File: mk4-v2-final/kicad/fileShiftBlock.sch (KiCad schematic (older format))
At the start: 2 parts, among them U4 74HC595, U5 74HC595

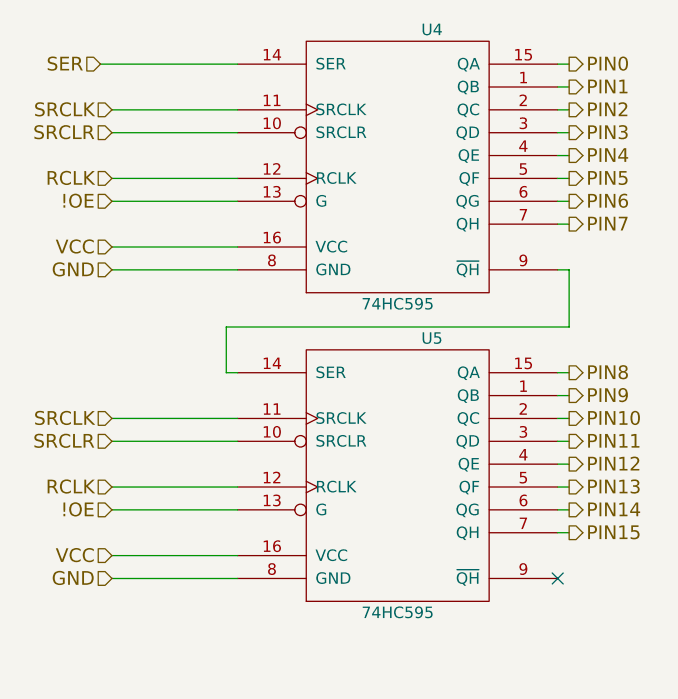
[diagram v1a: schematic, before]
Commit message: added headnight diodes, I don't think software control of them is going to be possible
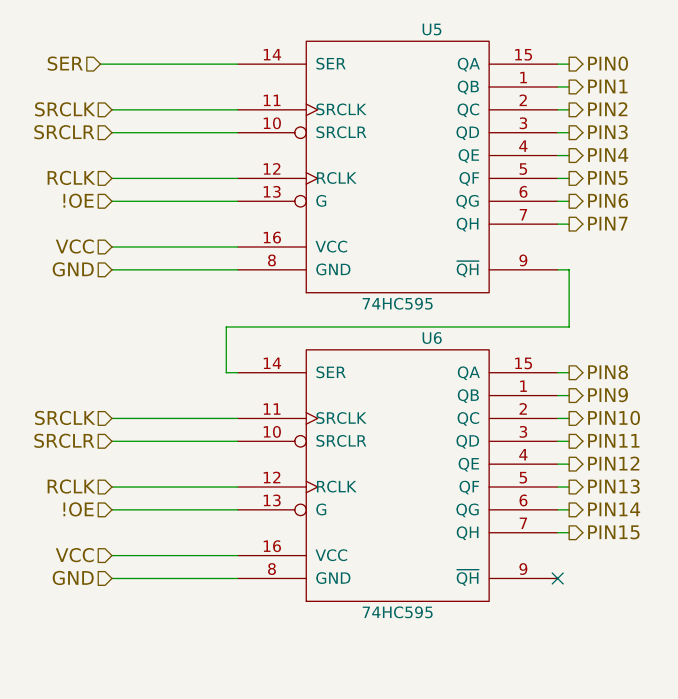
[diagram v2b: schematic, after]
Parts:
- renumbered U4 to U5, U5 to U6
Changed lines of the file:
@@
 $EndDescr
 $Comp
-L 74HC595-RESCUE-hitchco-mk4 U4
+L 74HC595-RESCUE-hitchco-mk4 U5
 U 1 1 5A664EEF
 P 5300 2950
-F 0 "U4" H 5450 3550 50  0000 C CNN
+F 0 "U5" H 5450 3550 50  0000 C CNN
 F 1 "74HC595" H 5300 2350 50  0000 C CNN
 F 2 "Housings_DIP:DIP-16_W7.62mm" H 5300 2950 50  0001 C CNN
@@
 	4600 3300 4050 3300
 $Comp
-L 74HC595-RESCUE-hitchco-mk4 U5
+L 74HC595-RESCUE-hitchco-mk4 U6
 U 1 1 5A26CD88
 P 5300 4300
-F 0 "U5" H 5450 4900 50  0000 C CNN
+F 0 "U6" H 5450 4900 50  0000 C CNN
 F 1 "74HC595" H 5300 3700 50  0000 C CNN
 F 2 "Housings_DIP:DIP-16_W7.62mm" H 5300 4300 50  0001 C CNN

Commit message: schematic is done, footprint association and netlist are also done
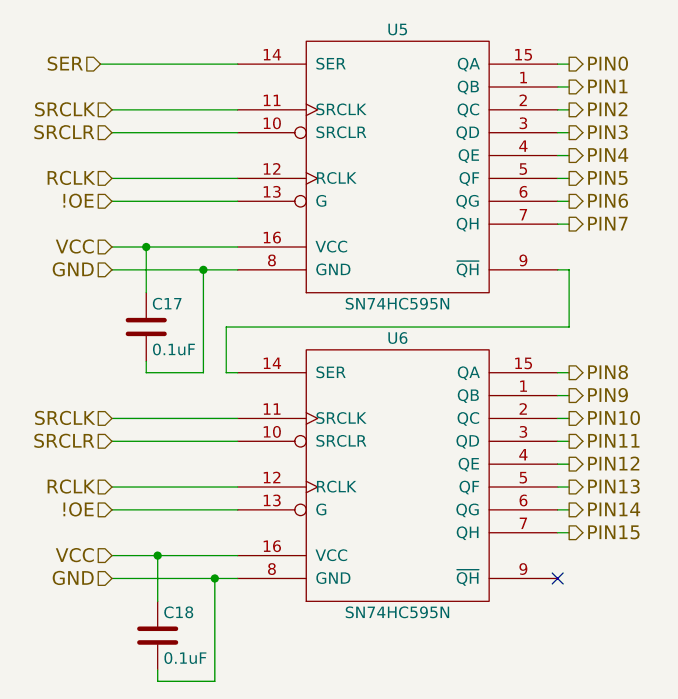
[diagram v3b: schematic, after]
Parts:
- removed U5, U6: 74HC595, Housings_DIP:DIP-16_W7.62mm, symbol 74HC595-RESCUE-hitchco-mk4
- added C17, C18: 0.1uF, C_Rect_L5.08mm_W3.175mm_P2.54mm:C_Rect_L5.08mm_W3.175mm_P2.54mm, symbol C
- added U5, U6: SN74HC595N, Housings_DIP:DIP-16_W7.62mm_Socket, symbol SN74HC595N
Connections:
- net !OE: now also U5.13 (G), U6.13 (G)
- net GND: now also C17.2, C18.2, U5.8 (GND), U6.8 (GND)
- net PIN0: now also U5.15 (QA)
- net PIN1: now also U5.1 (QB)
- net PIN10: now also U6.2 (QC)
- net PIN11: now also U6.3 (QD)
- net PIN12: now also U6.4 (QE)
- net PIN13: now also U6.5 (QF)
- net PIN14: now also U6.6 (QG)
- net PIN15: now also U6.7 (QH)
- net PIN2: now also U5.2 (QC)
- net PIN3: now also U5.3 (QD)
- net PIN4: now also U5.4 (QE)
- net PIN5: now also U5.5 (QF)
- net PIN6: now also U5.6 (QG)
- net PIN7: now also U5.7 (QH)
- net PIN8: now also U6.15 (QA)
- net PIN9: now also U6.1 (QB)
- net RCLK: now also U5.12 (RCLK), U6.12 (RCLK)
- net SER: now also U5.14 (SER)
- net SRCLK: now also U5.11 (SRCLK), U6.11 (SRCLK)
- net SRCLR: now also U5.10 (SRCLR), U6.10 (SRCLR)
- net VCC: now also C17.1, C18.1, U5.16 (VCC), U6.16 (VCC)
- new net: U5.9 (~QH), U6.14 (SER)
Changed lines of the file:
@@
 EESchema Schematic File Version 2
-LIBS:hitchco-mk4-rescue
 LIBS:power
 LIBS:device
@@
 LIBS:cd4013b
 LIBS:ncs3s1205sc
+LIBS:lca715
+LIBS:SN74HC595N
+LIBS:CD74HC4067
 LIBS:hitchco-mk4-cache
 EELAYER 25 0
@@
 $Descr A4 11693 8268
 encoding utf-8
-Sheet 45 54
+Sheet 38 54
 Title ""
 Date ""
@@
 $EndDescr
 $Comp
-L 74HC595-RESCUE-hitchco-mk4 U5
-U 1 1 5A664EEF
-P 5300 2950
-F 0 "U5" H 5450 3550 50  0000 C CNN
-F 1 "74HC595" H 5300 2350 50  0000 C CNN
-F 2 "Housings_DIP:DIP-16_W7.62mm" H 5300 2950 50  0001 C CNN
-F 3 "http://www.ti.com/lit/ds/symlink/sn74hc595.pdf" H 5300 2950 50  0001 C CNN
-	1    5300 2950
+L C C17
+U 1 1 5B1F2E84
+P 4200 3650
+F 0 "C17" H 4225 3750 50  0000 L CNN
+F 1 "0.1uF" H 4225 3550 50  0000 L CNN
+F 2 "C_Rect_L5.08mm_W3.175mm_P2.54mm:C_Rect_L5.08mm_W3.175mm_P2.54mm" H 4238 3500 50  0001 C CNN
+F 3 "http://datasheets.avx.com/AR-Series.pdf" H 4200 3650 50  0001 C CNN
+F 4 "478-5096-ND" H 4225 3850 50  0001 C CNN "digikey-pn"
+F 5 "AR205F104K4R" H 4225 3850 50  0001 C CNN "mfg-pn"
+	1    4200 3650
+	1    0    0    -1
+$EndComp
+$Comp
+L C C18
+U 1 1 5B1F2F7D
+P 4250 5000
+F 0 "C18" H 4275 5100 50  0000 L CNN
+F 1 "0.1uF" H 4275 4900 50  0000 L CNN
+F 2 "C_Rect_L5.08mm_W3.175mm_P2.54mm:C_Rect_L5.08mm_W3.175mm_P2.54mm" H 4288 4850 50  0001 C CNN
+F 3 "http://datasheets.avx.com/AR-Series.pdf" H 4250 5000 50  0001 C CNN
+F 4 "478-5096-ND" H 4275 5200 50  0001 C CNN "digikey-pn"
+F 5 "AR205F104K4R" H 4275 5200 50  0001 C CNN "mfg-pn"
+	1    4250 5000
 	1    0    0    -1
 $EndComp
@@
 Text HLabel 6050 3200 2    60   Output ~ 0
 PIN7
-Wire Wire Line
-	6000 3400 6050 3400
-Wire Wire Line
-	6050 3400 6050 3650
-Wire Wire Line
-	6050 3650 4550 3650
-Wire Wire Line
-	4550 3650 4550 3850
-Wire Wire Line
-	4550 3850 4600 3850
 Text HLabel 6050 3850 2    60   Output ~ 0
 PIN8
@@
 Text HLabel 6050 4550 2    60   Output ~ 0
 PIN15
-Wire Wire Line
-	6050 2500 6000 2500
-Wire Wire Line
-	6000 2600 6050 2600
-Wire Wire Line
-	6050 2700 6000 2700
-Wire Wire Line
-	6000 2800 6050 2800
-Wire Wire Line
-	6050 2900 6000 2900
-Wire Wire Line
-	6000 3000 6050 3000
-Wire Wire Line
-	6050 3100 6000 3100
-Wire Wire Line
-	6000 3200 6050 3200
-Wire Wire Line
-	6000 3950 6050 3950
-Wire Wire Line
-	6050 4050 6000 4050
-Wire Wire Line
-	6000 4150 6050 4150
-Wire Wire Line
-	6050 4250 6000 4250
-Wire Wire Line
-	6000 4350 6050 4350
-Wire Wire Line
-	6050 4450 6000 4450
-Wire Wire Line
-	6000 4550 6050 4550
 Text HLabel 4000 2500 0    60   Input ~ 0
 SER
-Wire Wire Line
-	4000 2500 4600 2500
 Text HLabel 4050 2700 0    60   Input ~ 0
 SRCLK
-Wire Wire Line
-	4050 2800 4600 2800
 Text HLabel 4050 3000 0    60   Input ~ 0
 RCLK
-Wire Wire Line
-	4050 3000 4600 3000
-Wire Wire Line
-	4050 2700 4600 2700
 Text HLabel 4050 2800 0    60   Input ~ 0
 SRCLR
 Text HLabel 4050 3100 0    60   Input ~ 0
 !OE
-Wire Wire Line
-	4050 3100 4600 3100
 Text HLabel 4050 3300 0    60   Input ~ 0
 VCC
 Text HLabel 4050 3400 0    60   Input ~ 0
 GND
-Wire Wire Line
-	4050 3400 4600 3400
-Wire Wire Line
-	4600 3300 4050 3300
-$Comp
-L 74HC595-RESCUE-hitchco-mk4 U6
-U 1 1 5A26CD88
-P 5300 4300
-F 0 "U6" H 5450 4900 50  0000 C CNN
-F 1 "74HC595" H 5300 3700 50  0000 C CNN
-F 2 "Housings_DIP:DIP-16_W7.62mm" H 5300 4300 50  0001 C CNN
-F 3 "http://www.ti.com/lit/ds/symlink/sn74hc595.pdf" H 5300 4300 50  0001 C CNN
-	1    5300 4300
-	1    0    0    -1
-$EndComp
 Text HLabel 4050 4050 0    60   Input ~ 0
 SRCLK
-Wire Wire Line
-	4050 4150 4600 4150
 Text HLabel 4050 4350 0    60   Input ~ 0
 RCLK
-Wire Wire Line
-	4050 4350 4600 4350
-Wire Wire Line
-	4050 4050 4600 4050
 Text HLabel 4050 4150 0    60   Input ~ 0
 SRCLR
 Text HLabel 4050 4450 0    60   Input ~ 0
 !OE
-Wire Wire Line
-	4050 4450 4600 4450
 Text HLabel 4050 4650 0    60   Input ~ 0
 VCC
@@
 GND
 Wire Wire Line
+	6000 3400 6050 3400
+Wire Wire Line
+	6050 3400 6050 3650
+Wire Wire Line
+	6050 3650 4550 3650
+Wire Wire Line
+	4550 3650 4550 3850
+Wire Wire Line
+	4550 3850 4600 3850
+Wire Wire Line
+	6050 2500 6000 2500
+Wire Wire Line
+	6000 2600 6050 2600
+Wire Wire Line
+	6050 2700 6000 2700
+Wire Wire Line
+	6000 2800 6050 2800
+Wire Wire Line
+	6050 2900 6000 2900
+Wire Wire Line
+	6000 3000 6050 3000
+Wire Wire Line
+	6050 3100 6000 3100
+Wire Wire Line
+	6000 3200 6050 3200
+Wire Wire Line
+	6000 3950 6050 3950
+Wire Wire Line
+	6050 4050 6000 4050
+Wire Wire Line
+	6000 4150 6050 4150
+Wire Wire Line
+	6050 4250 6000 4250
+Wire Wire Line
+	6000 4350 6050 4350
+Wire Wire Line
+	6050 4450 6000 4450
+Wire Wire Line
+	6000 4550 6050 4550
+Wire Wire Line
+	4000 2500 4600 2500
+Wire Wire Line
+	4050 2800 4600 2800
+Wire Wire Line
+	4050 3000 4600 3000
+Wire Wire Line
+	4050 2700 4600 2700
+Wire Wire Line
+	4050 3100 4600 3100
+Wire Wire Line
+	4050 3400 4600 3400
+Wire Wire Line
+	4600 3300 4050 3300
+Wire Wire Line
+	4050 4150 4600 4150
+Wire Wire Line
+	4050 4350 4600 4350
+Wire Wire Line
+	4050 4050 4600 4050
+Wire Wire Line
+	4050 4450 4600 4450
+Wire Wire Line
 	4050 4750 4600 4750
 Wire Wire Line
@@
 Wire Wire Line
 	6050 3850 6000 3850
+Wire Wire Line
+	4200 3500 4200 3300
+Wire Wire Line
+	4200 3800 4200 3850
+Wire Wire Line
+	4200 3850 4450 3850
+Wire Wire Line
+	4450 3850 4450 3400
+Wire Wire Line
+	4250 4850 4250 4650
+Wire Wire Line
+	4250 5150 4250 5200
+Wire Wire Line
+	4250 5200 4500 5200
+Wire Wire Line
+	4500 5200 4500 4750
+Connection ~ 4200 3300
+Connection ~ 4450 3400
+Connection ~ 4250 4650
+Connection ~ 4500 4750
 NoConn ~ 6000 4750
+$Comp
+L SN74HC595N U5
+U 1 1 5B11D691
+P 5300 2950
+F 0 "U5" H 5300 3550 50  0000 C CNN
+F 1 "SN74HC595N" H 5300 2350 50  0000 C CNN
+F 2 "Housings_DIP:DIP-16_W7.62mm_Socket" H 5300 2950 50  0001 C CNN
+F 3 "http://www.ti.com/lit/ds/symlink/sn74hc595.pdf" H 5300 2950 50  0001 C CNN
+F 4 "SN74HC595N" H 5300 2950 60  0001 C CNN "mfg-pn"
+F 5 "296-1600-5-ND" H 5300 2950 60  0001 C CNN "digikey-pn"
+	1    5300 2950
+	1    0    0    -1
+$EndComp
+$Comp
+L SN74HC595N U6
+U 1 1 5B11D9E3
+P 5300 4300
+F 0 "U6" H 5300 4900 50  0000 C CNN
+F 1 "SN74HC595N" H 5300 3700 50  0000 C CNN
+F 2 "Housings_DIP:DIP-16_W7.62mm_Socket" H 5300 4300 50  0001 C CNN
+F 3 "http://www.ti.com/lit/ds/symlink/sn74hc595.pdf" H 5300 4300 50  0001 C CNN
+F 4 "SN74HC595N" H 5300 4300 60  0001 C CNN "mfg-pn"
+F 5 "296-1600-5-ND" H 5300 4300 60  0001 C CNN "digikey-pn"
+	1    5300 4300
+	1    0    0    -1
+$EndComp
 $EndSCHEMATC
